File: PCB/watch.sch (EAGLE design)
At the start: 60 parts, among them IC1 ISL1209, J2 USB-MICROB, Q1 32.768 KHz, T1 BC850, U2 MKL27Z256VLH4

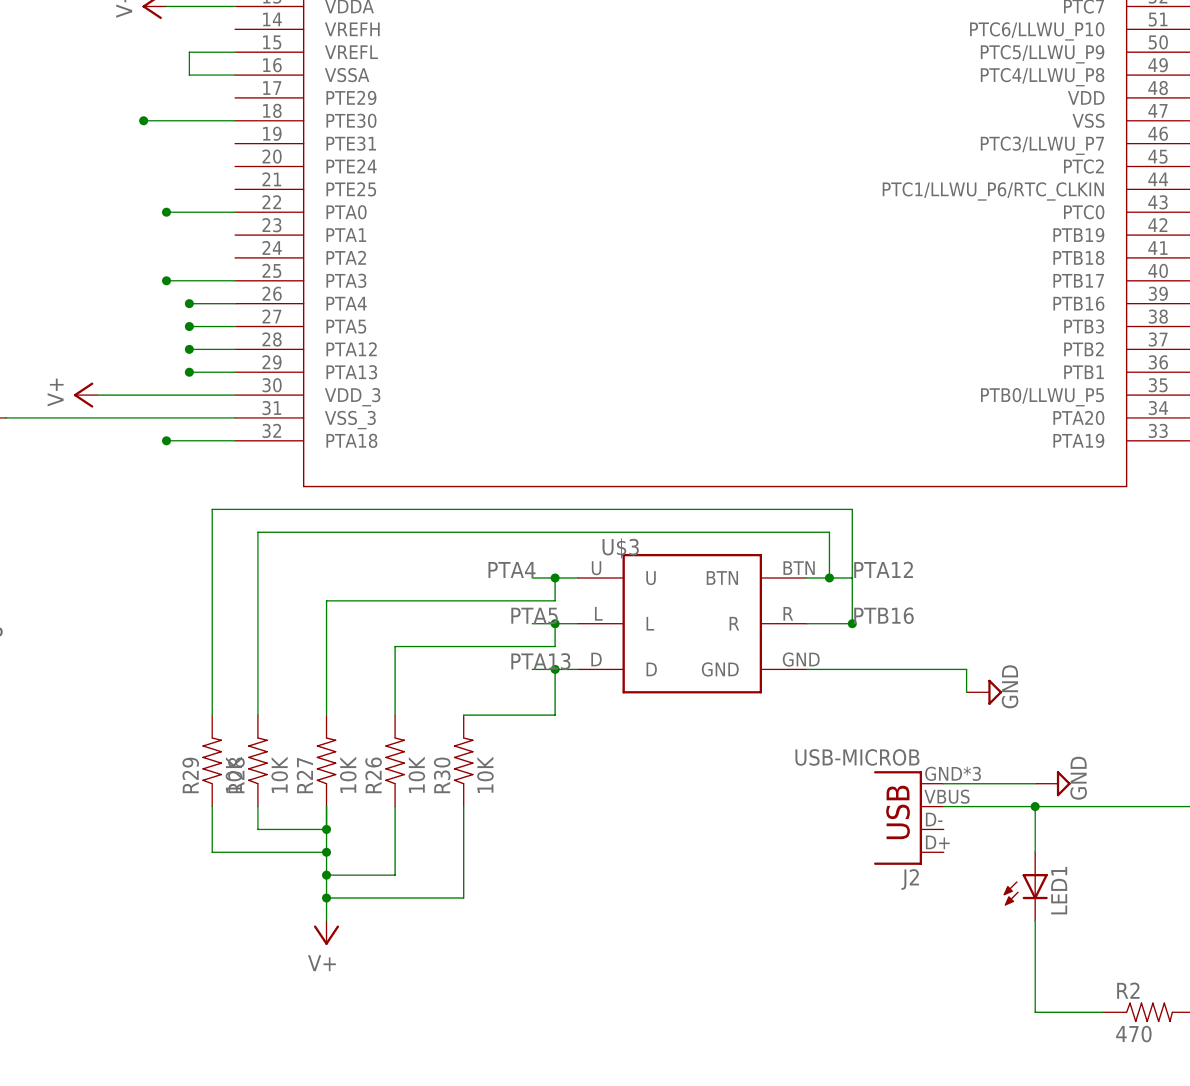
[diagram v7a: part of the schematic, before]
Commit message: added dip switches. need to check spaces for compass.
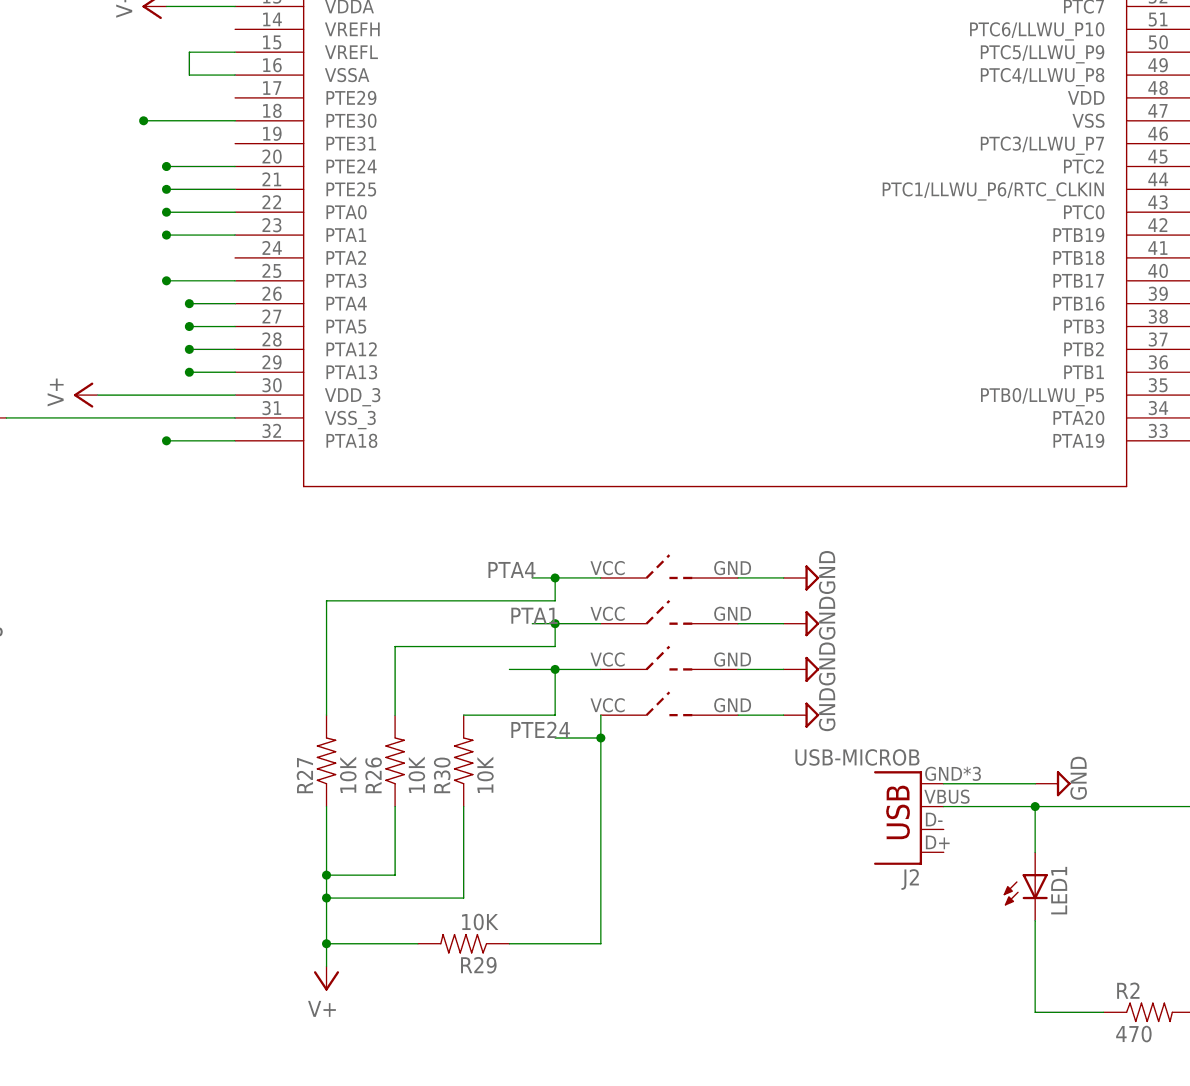
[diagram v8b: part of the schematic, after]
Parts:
- removed R28: 10K, SparkFun-Resistors:RESISTOR0603
- added U$7, U$8, U$9: DIPS, BOS_libs:DIPS
- U$3: value 5-WAYSWITCH -> DIPS; device 5-wayswitch:5-WAYSWITCH -> BOS_libs:DIPS
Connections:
- new net PTA1: R26.2, U$7.V, U2.PTA1
- new net PTE24: R29.1, U$9.V, U2.PTE24
- new net PTE25: R30.2, U$8.V, U2.PTE25
- net GND: now also U$7.GND, U$8.GND, U$9.GND
- net PTA12: no longer R28.2, U$3.BTN
- net PTA13: no longer R30.2, U$3.D
- net PTA4: now also U$3.V; no longer U$3.U
- net PTA5: no longer R26.2, U$3.L
- net PTB16: no longer R29.2, U$3.R
- net V+: now also R29.2; no longer R28.1, R29.1
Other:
- moved on the sheet: R29
